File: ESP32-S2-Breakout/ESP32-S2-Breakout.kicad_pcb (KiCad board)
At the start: 2 copper layers, 55.9 x 30.5 mm, 37 parts, among them J1 USB_B_Micro, J2 Conn_01x21, J3 Conn_01x21, SW1 Reset, SW2 Boot, U1 USBLC6-2SC6, U2 ESP32-S2-WROOM, U3 XC6220B331MR, Y1 32.768KHz

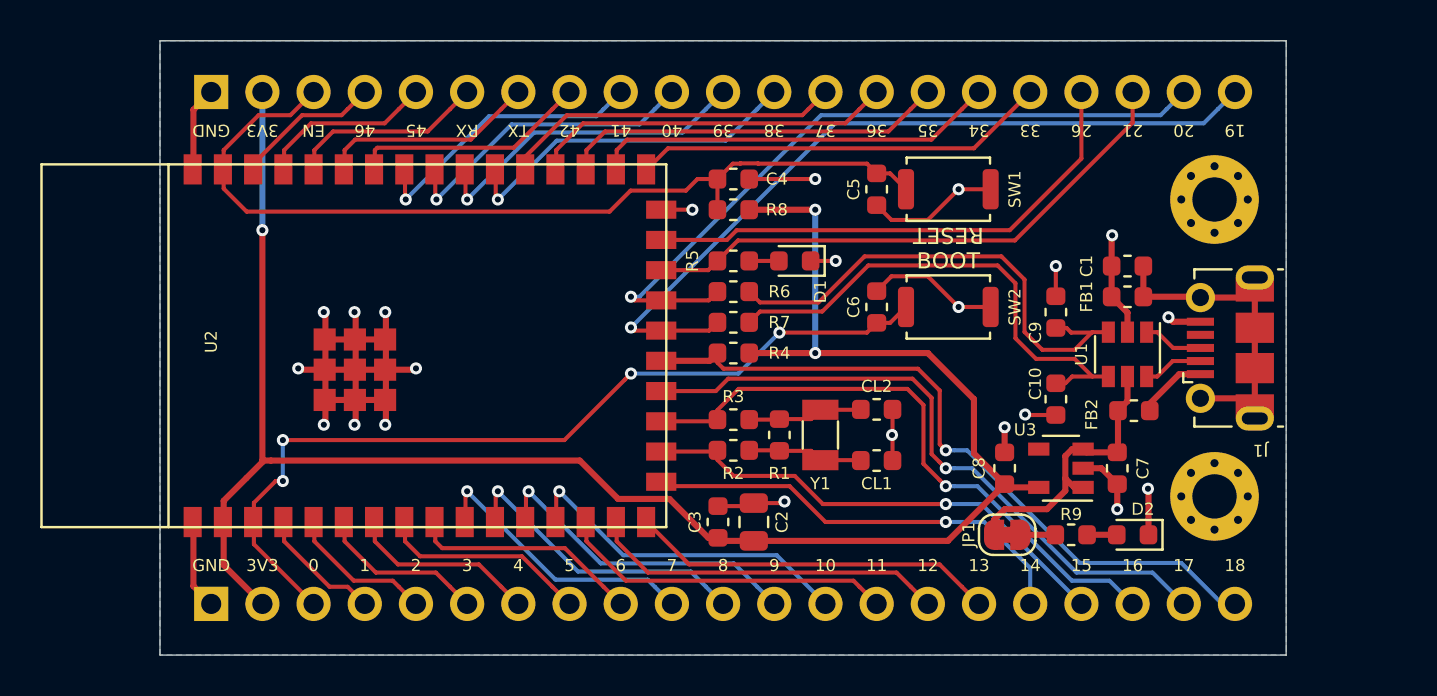
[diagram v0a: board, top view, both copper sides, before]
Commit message: Add 5v and extra gnd pin to pin headers, rearrange pcb
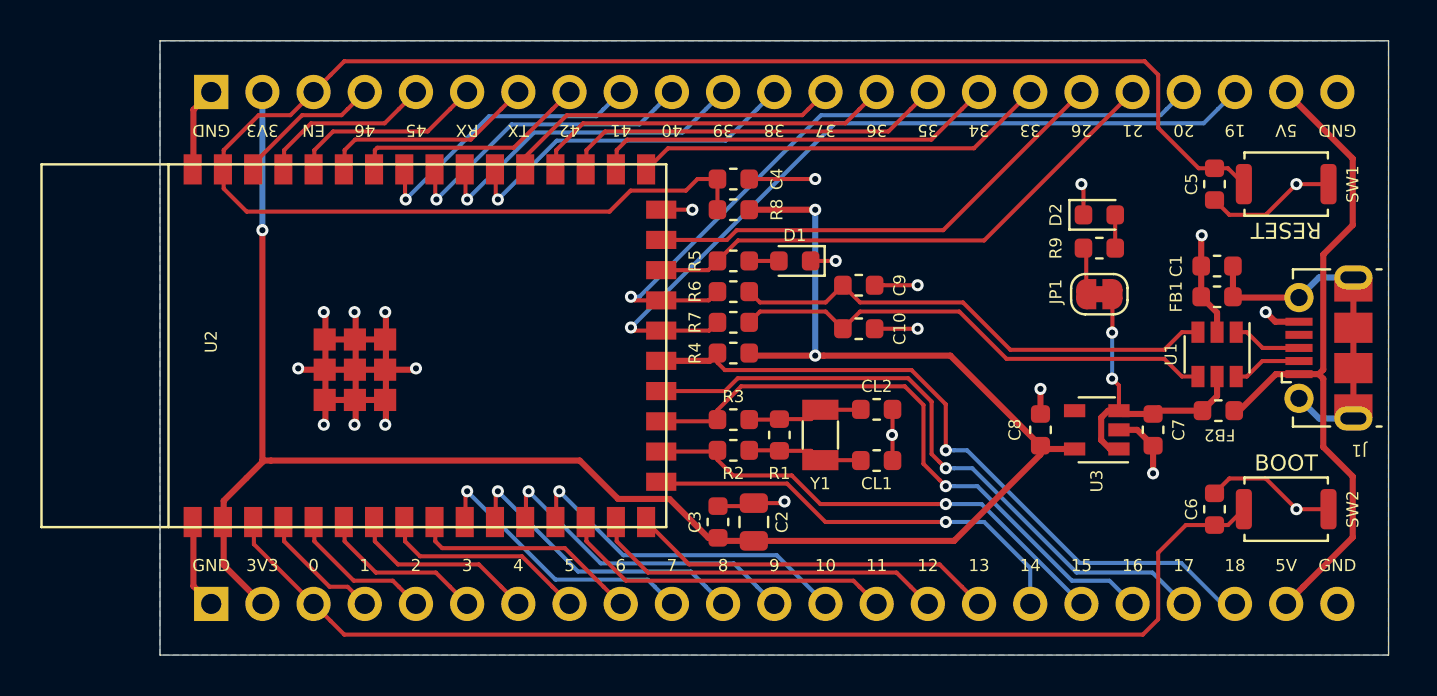
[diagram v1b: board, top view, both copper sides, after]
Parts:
- removed H1, H2: MountingHole, MountingHole:MountingHole_2.2mm_M2_Pad_Via
- removed J2: Conn_01x21, Connector_PinHeader_2.54mm:PinHeader_1x21_P2.54mm_Vertical
- added e1: Conn_01x23, Connector_PinHeader_2.54mm:PinHeader_1x23_P2.54mm_Vertical, B.Cu at (119.4, 111.8)
- J3: value Conn_01x21 -> Conn_01x23; footprint Connector_PinHeader_2.54mm:PinHeader_1x21_P2.54mm_Vertical -> Connector_PinHeader_2.54mm:PinHeader_1x23_P2.54mm_Vertical
- moved SW2 19.5 mm to (172.7, 107.1)
- moved C6 19.5 mm to (169.2, 107.1)
- moved SW1 16.8 mm to (172.7, 90.9)
- moved C5 16.8 mm to (169.2, 90.9)
- moved D2 16.0 mm to (163.4, 92.5), turned to 0 degrees
- moved R9 14.3 mm to (163.4, 94.1)
- moved JP1 12.8 mm to (163.4, 96.4), turned to 180 degrees
- moved C10 10.4 mm to (151.5, 98.1), turned to 0 degrees
- moved C9 9.87 mm to (151.5, 95.9), turned to 180 degrees
- moved J1 4.89 mm to (174.8, 99.1)
- moved C1 4.44 mm to (169.3, 95.0)
- moved FB1 4.44 mm to (169.3, 96.5)
- moved U1 4.44 mm to (169.3, 99.4)
- moved FB2 4.19 mm to (169.4, 102.2)
- moved C7 2.61 mm to (166.1, 103.1)
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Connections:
- FB2 pad 2: Net-(FB2-Pad2) -> +5V
- J1 pad 1: Net-(FB2-Pad2) -> +5V
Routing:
- net /EN: track 44.9 -> 85.6 mm
- net +5V: track 0.00 -> 34.2 mm
- net /IO0: track 43.8 -> 56.6 mm, vias 4 -> 0
- net Net-(FB2-Pad2): track 3.47 -> 0.00 mm
- net +3V3: track 95.5 -> 97.9 mm
- net /IO26: track 25.8 -> 23.9 mm
- net VBUS: track 14.8 -> 15.8 mm, vias 0 -> 2
- net /IO21: track 28.2 -> 27.3 mm
- net GND: track 79.3 -> 80.1 mm
- net Net-(JP1-Pad2): track 1.74 -> 2.34 mm
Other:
- board size 55.9 x 30.5 mm -> 61 x 30.5 mm
- board text added: "5V"

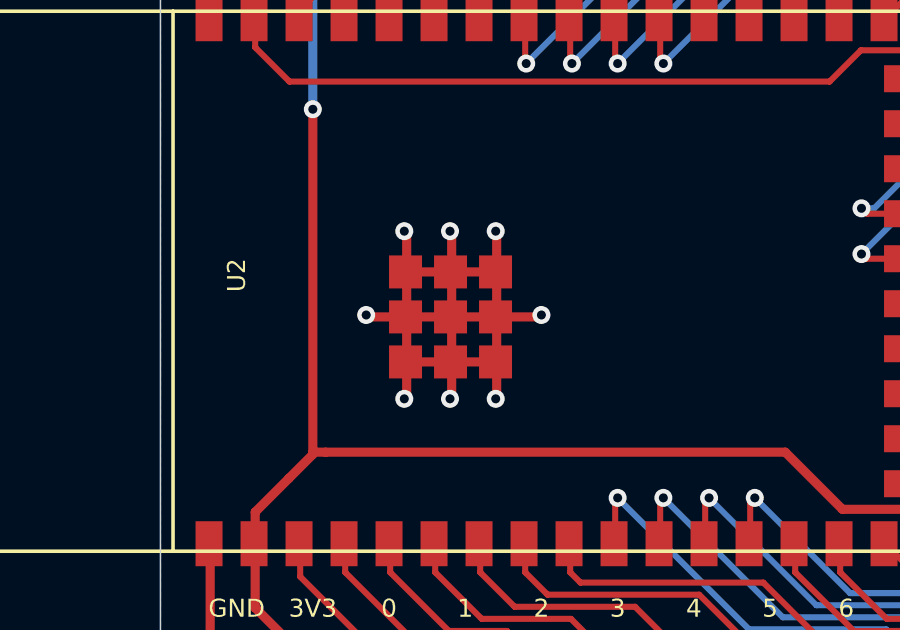
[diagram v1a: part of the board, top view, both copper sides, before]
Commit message: Added copper pour around EPAD
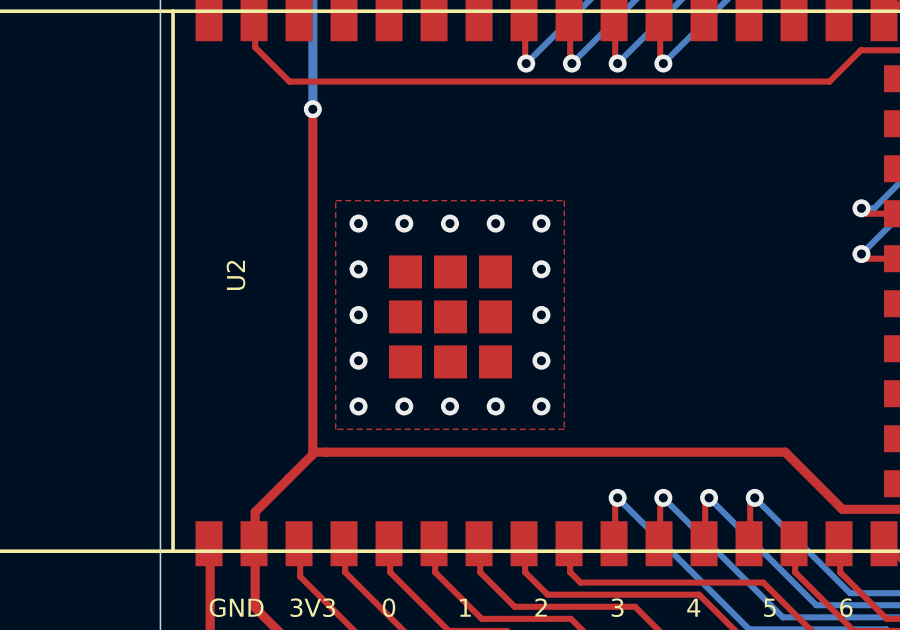
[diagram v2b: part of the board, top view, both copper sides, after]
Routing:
- net GND: track 80.1 -> 51.3 mm, vias 22 -> 30
- added copper zone on F.Cu, net GND
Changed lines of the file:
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@@
     (thickness 1.6)
     (drawings 102)
-    (tracks 472)
+    (tracks 452)
     (zones 0)
     (modules 35)
@@
   )
   (setup
-    (last_trace_width 0.25)
+    (last_trace_width 0.3048)
     (user_trace_width 0.2032)
     (user_trace_width 0.3048)
+    (user_trace_width 0.508)
     (trace_clearance 0.2)
     (zone_clearance 0.254)
@@
   (gr_line (start 116.84 114.3) (end 177.8 114.3) (layer Edge.Cuts) (width 0.05))
   (gr_line (start 116.84 83.82) (end 116.84 114.3) (layer Edge.Cuts) (width 0.05))
+  (via (at 129.54 97.028) (size 0.6) (drill 0.3) (layers F.Cu B.Cu) (net 2))
+  (via (at 123.444 97.028) (size 0.6) (drill 0.3) (layers F.Cu B.Cu) (net 2))
+  (via (at 123.444 103.124) (size 0.6) (drill 0.3) (layers F.Cu B.Cu) (net 2))
+  (via (at 129.54 103.124) (size 0.6) (drill 0.3) (layers F.Cu B.Cu) (net 2))
+  (via (at 129.54 98.552) (size 0.6) (drill 0.3) (layers F.Cu B.Cu) (net 2))
+  (via (at 129.54 101.6) (size 0.6) (drill 0.3) (layers F.Cu B.Cu) (net 2))
+  (via (at 123.444 101.6) (size 0.6) (drill 0.3) (layers F.Cu B.Cu) (net 2))
+  (via (at 123.444 98.552) (size 0.6) (drill 0.3) (layers F.Cu B.Cu) (net 2))
   (segment (start 121.498 108.798) (end 124.46 111.76) (width 0.2032) (layer F.Cu) (net 1))
   (segment (start 121.498 107.7) (end 121.498 108.798) (width 0.2032) (layer F.Cu) (net 1))
@@
   (segment (start 153.1875 103.3525) (end 153.162 103.378) (width 0.2032) (layer F.Cu) (net 2))
   (segment (start 153.1875 102.108) (end 153.1875 103.3525) (width 0.2032) (layer F.Cu) (net 2))
-  (via (at 124.968 102.87) (size 0.6) (drill 0.3) (layers F.Cu B.Cu) (net 2))
-  (segment (start 125.048 102.79) (end 124.968 102.87) (width 0.3048) (layer F.Cu) (net 2))
-  (segment (start 125.048 101.64) (end 125.048 102.79) (width 0.3048) (layer F.Cu) (net 2))
-  (via (at 124.968 97.282) (size 0.6) (drill 0.3) (layers F.Cu B.Cu) (net 2))
-  (segment (start 125.048 97.362) (end 124.968 97.282) (width 0.3048) (layer F.Cu) (net 2))
-  (segment (start 125.048 98.64) (end 125.048 97.362) (width 0.3048) (layer F.Cu) (net 2))
-  (via (at 126.492 102.87) (size 0.6) (drill 0.3) (layers F.Cu B.Cu) (net 2))
-  (segment (start 126.548 102.814) (end 126.492 102.87) (width 0.3048) (layer F.Cu) (net 2))
-  (segment (start 126.548 101.64) (end 126.548 102.814) (width 0.3048) (layer F.Cu) (net 2))
-  (segment (start 126.548 97.338) (end 126.492 97.282) (width 0.3048) (layer F.Cu) (net 2))
-  (via (at 126.492 97.282) (size 0.6) (drill 0.3) (layers F.Cu B.Cu) (net 2))
-  (segment (start 126.548 98.64) (end 126.548 97.338) (width 0.3048) (layer F.Cu) (net 2))
-  (via (at 128.016 102.87) (size 0.6) (drill 0.3) (layers F.Cu B.Cu) (net 2))
-  (segment (start 128.048 102.838) (end 128.016 102.87) (width 0.3048) (layer F.Cu) (net 2))
-  (segment (start 128.048 101.64) (end 128.048 102.838) (width 0.3048) (layer F.Cu) (net 2))
-  (via (at 128.016 97.282) (size 0.6) (drill 0.3) (layers F.Cu B.Cu) (net 2))
-  (segment (start 128.048 97.314) (end 128.016 97.282) (width 0.3048) (layer F.Cu) (net 2))
-  (segment (start 128.048 98.64) (end 128.048 97.314) (width 0.3048) (layer F.Cu) (net 2))
-  (segment (start 125.048 101.64) (end 125.048 100.14) (width 0.3048) (layer F.Cu) (net 2))
-  (segment (start 125.048 98.64) (end 125.048 100.14) (width 0.3048) (layer F.Cu) (net 2))
-  (segment (start 126.548 100.14) (end 126.548 101.64) (width 0.3048) (layer F.Cu) (net 2))
-  (segment (start 126.548 98.64) (end 126.548 100.14) (width 0.3048) (layer F.Cu) (net 2))
-  (segment (start 128.048 100.14) (end 128.048 101.64) (width 0.3048) (layer F.Cu) (net 2))
-  (segment (start 128.048 98.64) (end 128.048 100.14) (width 0.3048) (layer F.Cu) (net 2))
-  (segment (start 125.048 101.64) (end 126.548 101.64) (width 0.3048) (layer F.Cu) (net 2))
-  (segment (start 125.048 100.14) (end 126.548 100.14) (width 0.3048) (layer F.Cu) (net 2))
-  (segment (start 125.048 98.64) (end 126.548 98.64) (width 0.3048) (layer F.Cu) (net 2))
-  (segment (start 128.048 98.64) (end 126.548 98.64) (width 0.3048) (layer F.Cu) (net 2))
-  (segment (start 128.048 100.14) (end 126.548 100.14) (width 0.3048) (layer F.Cu) (net 2))
-  (segment (start 128.048 101.64) (end 126.548 101.64) (width 0.3048) (layer F.Cu) (net 2))
+  (via (at 124.968 103.124) (size 0.6) (drill 0.3) (layers F.Cu B.Cu) (net 2))
+  (via (at 124.968 97.028) (size 0.6) (drill 0.3) (layers F.Cu B.Cu) (net 2))
+  (via (at 126.492 103.124) (size 0.6) (drill 0.3) (layers F.Cu B.Cu) (net 2))
+  (via (at 126.492 97.028) (size 0.6) (drill 0.3) (layers F.Cu B.Cu) (net 2))
+  (via (at 128.016 103.124) (size 0.6) (drill 0.3) (layers F.Cu B.Cu) (net 2))
+  (via (at 128.016 97.028) (size 0.6) (drill 0.3) (layers F.Cu B.Cu) (net 2))
   (via (at 173.228 107.061) (size 0.6) (drill 0.3) (layers F.Cu B.Cu) (net 2))
   (segment (start 169.164 106.2735) (end 169.9005 105.537) (width 0.2032) (layer F.Cu) (net 2))
@@
   (via (at 150.367996 94.742) (size 0.6) (drill 0.3) (layers F.Cu B.Cu) (net 2))
   (segment (start 149.1235 94.742) (end 150.367996 94.742) (width 0.2032) (layer F.Cu) (net 2))
-  (via (at 123.698 100.076) (size 0.6) (drill 0.3) (layers F.Cu B.Cu) (net 2))
-  (segment (start 123.762 100.14) (end 123.698 100.076) (width 0.3048) (layer F.Cu) (net 2))
-  (segment (start 125.048 100.14) (end 123.762 100.14) (width 0.3048) (layer F.Cu) (net 2))
+  (via (at 123.444 100.076) (size 0.6) (drill 0.3) (layers F.Cu B.Cu) (net 2))
   (via (at 129.54 100.076) (size 0.6) (drill 0.3) (layers F.Cu B.Cu) (net 2))
-  (segment (start 128.048 100.14) (end 129.476 100.14) (width 0.3048) (layer F.Cu) (net 2))
-  (segment (start 129.476 100.14) (end 129.54 100.076) (width 0.3048) (layer F.Cu) (net 2))
   (segment (start 169.291 97.3075) (end 168.5035 96.52) (width 0.3048) (layer F.Cu) (net 2))
   (segment (start 169.291 98.2775) (end 169.291 97.3075) (width 0.3048) (layer F.Cu) (net 2))
@@
       )
     )
+  )
+  (zone (net 2) (net_name GND) (layer F.Cu) (hatch edge 0.508)
+    (connect_pads yes (clearance 0.254))
+    (min_thickness 0.254)
+    (fill yes (arc_segments 32) (thermal_gap 0.508) (thermal_bridge_width 0.508))
+    (polygon
+      (pts
+        (xy 130.302 103.886) (xy 122.682 103.886) (xy 122.682 96.266) (xy 130.302 96.266)
+      )
+    )

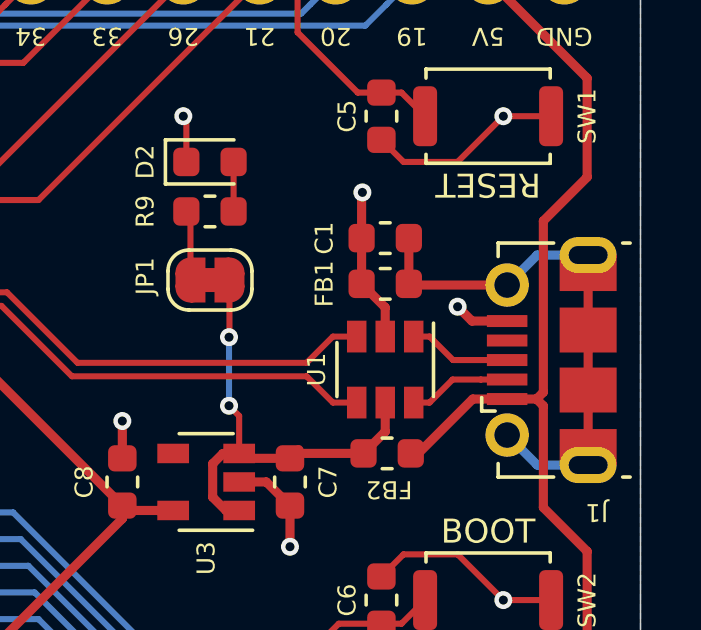
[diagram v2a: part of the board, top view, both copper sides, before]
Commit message: Add polarity marker to TVS
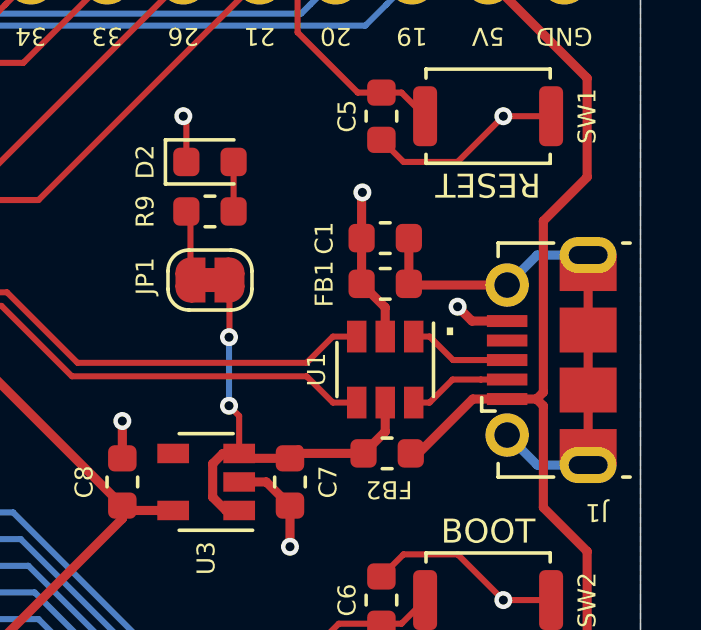
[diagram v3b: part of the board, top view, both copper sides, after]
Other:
- board text added: "."
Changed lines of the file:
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@@
-(kicad_pcb (version 20171130) (host pcbnew "(5.1.5)-3")
+(kicad_pcb (version 20171130) (host pcbnew "(5.1.5-0-10_14)")
   (general
     (thickness 1.6)
-    (drawings 102)
+    (drawings 103)
     (tracks 452)
     (zones 0)
@@
   )
   (setup
-    (last_trace_width 0.3048)
+    (last_trace_width 0.25)
     (user_trace_width 0.2032)
     (user_trace_width 0.3048)
@@
     )
   )
+  (gr_text . (at 171.45 97.536) (layer F.SilkS)
+    (effects (font (size 1.5 1.5) (thickness 0.3)))
+  )
   (gr_text GND (at 175.26 109.855) (layer B.SilkS)
     (effects (font (size 0.6 0.6) (thickness 0.15)) (justify mirror))
@@
   (gr_line (start 116.84 114.3) (end 177.8 114.3) (layer Edge.Cuts) (width 0.05))
   (gr_line (start 116.84 83.82) (end 116.84 114.3) (layer Edge.Cuts) (width 0.05))
-  (via (at 129.54 97.028) (size 0.6) (drill 0.3) (layers F.Cu B.Cu) (net 2))
-  (via (at 123.444 97.028) (size 0.6) (drill 0.3) (layers F.Cu B.Cu) (net 2))
-  (via (at 123.444 103.124) (size 0.6) (drill 0.3) (layers F.Cu B.Cu) (net 2))
-  (via (at 129.54 103.124) (size 0.6) (drill 0.3) (layers F.Cu B.Cu) (net 2))
-  (via (at 129.54 98.552) (size 0.6) (drill 0.3) (layers F.Cu B.Cu) (net 2))
-  (via (at 129.54 101.6) (size 0.6) (drill 0.3) (layers F.Cu B.Cu) (net 2))
-  (via (at 123.444 101.6) (size 0.6) (drill 0.3) (layers F.Cu B.Cu) (net 2))
-  (via (at 123.444 98.552) (size 0.6) (drill 0.3) (layers F.Cu B.Cu) (net 2))
   (segment (start 121.498 108.798) (end 124.46 111.76) (width 0.2032) (layer F.Cu) (net 1))
   (segment (start 121.498 107.7) (end 121.498 108.798) (width 0.2032) (layer F.Cu) (net 1))
@@
   (segment (start 166.37 112.522) (end 165.608 113.284) (width 0.2032) (layer F.Cu) (net 1))
   (segment (start 165.608 113.284) (end 125.984 113.284) (width 0.2032) (layer F.Cu) (net 1))
+  (via (at 129.54 97.028) (size 0.6) (drill 0.3) (layers F.Cu B.Cu) (net 2))
+  (via (at 123.444 97.028) (size 0.6) (drill 0.3) (layers F.Cu B.Cu) (net 2))
+  (via (at 123.444 103.124) (size 0.6) (drill 0.3) (layers F.Cu B.Cu) (net 2))
+  (via (at 129.54 103.124) (size 0.6) (drill 0.3) (layers F.Cu B.Cu) (net 2))
+  (via (at 129.54 98.552) (size 0.6) (drill 0.3) (layers F.Cu B.Cu) (net 2))
+  (via (at 129.54 101.6) (size 0.6) (drill 0.3) (layers F.Cu B.Cu) (net 2))
+  (via (at 123.444 101.6) (size 0.6) (drill 0.3) (layers F.Cu B.Cu) (net 2))
+  (via (at 123.444 98.552) (size 0.6) (drill 0.3) (layers F.Cu B.Cu) (net 2))
   (segment (start 118.498 87.242) (end 119.38 86.36) (width 0.3048) (layer F.Cu) (net 2))
   (segment (start 118.498 90.2) (end 118.498 87.242) (width 0.3048) (layer F.Cu) (net 2))
